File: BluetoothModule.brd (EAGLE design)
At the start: 58.4 x 30.5 mm, 25 parts, among them IC1 BL600, IC2 FT230XQ, J1 Autorun, J3 OTA, J6 USB

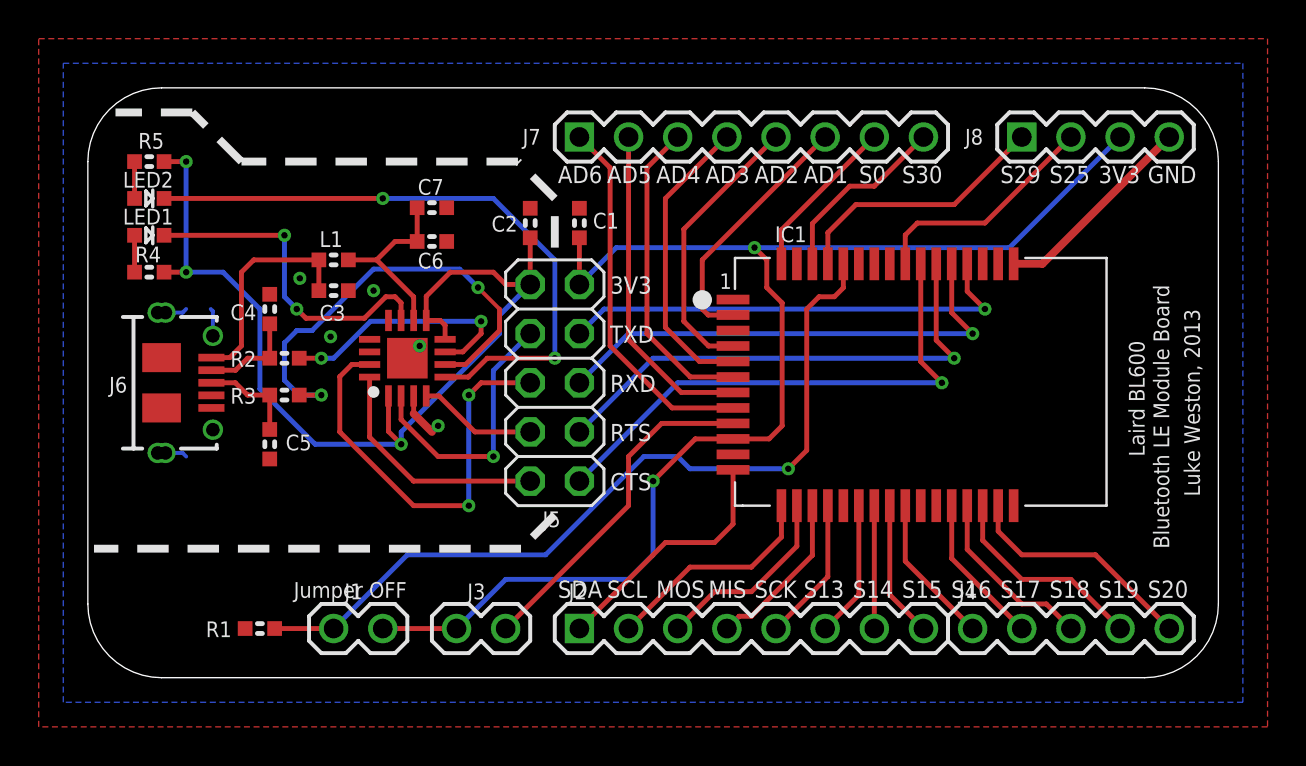
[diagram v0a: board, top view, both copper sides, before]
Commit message: tweaked USB connector footprint
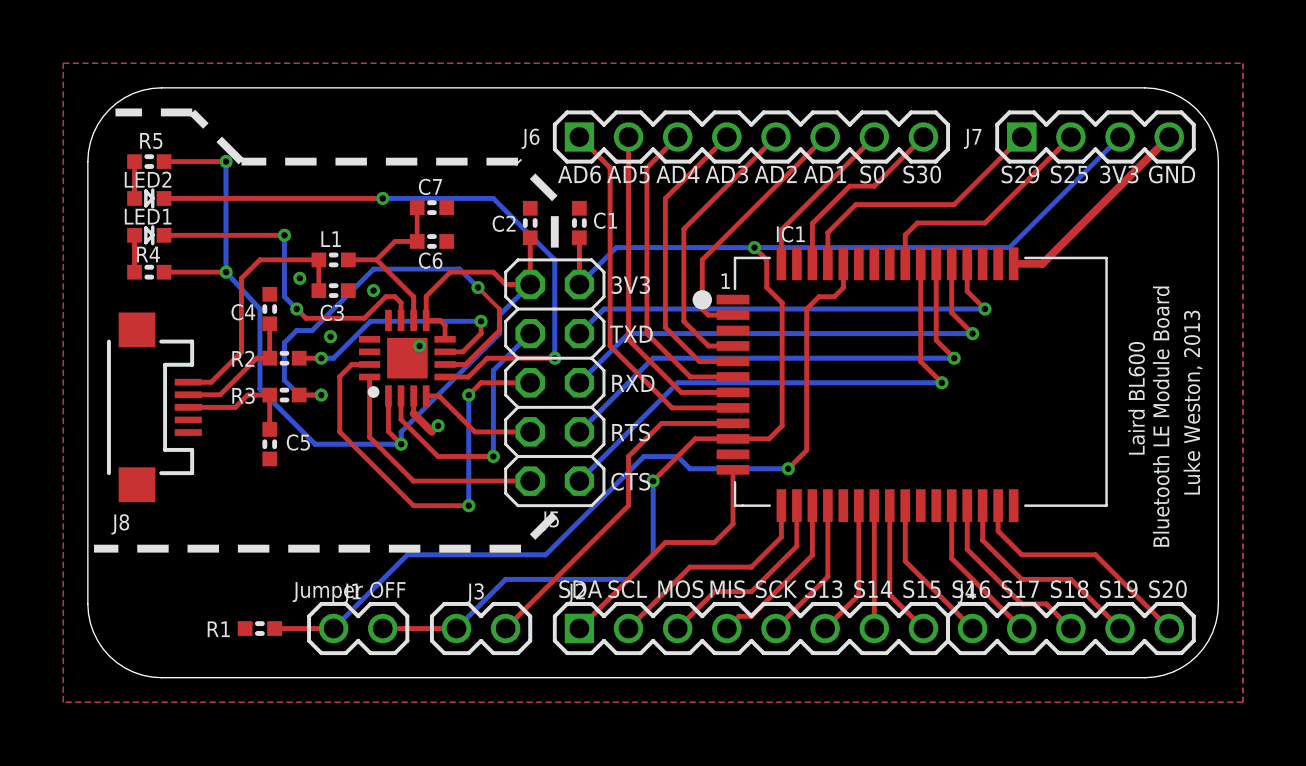
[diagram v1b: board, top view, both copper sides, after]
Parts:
- J6: value USB -> (none); device freetronics-jon:USB-MICROB-MB05PMXX -> freetronics-master-v1:1X08
- J7: device freetronics-master-v1:1X08 -> freetronics-master-v1:1X04
- J8: value (none) -> USB; device freetronics-master-v1:1X04 -> freetronics-master-v1:USB-MICROB
- moved J8 47.8 mm to (2.54, 14.0), turned to 270 degrees
- moved J6 25.0 mm to (25.4, 27.9), turned to 0 degrees
- moved J7 22.9 mm to (48.3, 27.9)
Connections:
- net +3V3: now also J7.3; no longer J8.3
- net ADC1: now also J6.6; no longer J7.6
- net ADC2: now also J6.5; no longer J7.5
- net ADC3: now also J6.4; no longer J7.4
- net ADC4: now also J6.3; no longer J7.3
- net ADC5: now also J6.2; no longer J7.2
- net ADC6: now also J6.1; no longer J7.1
- net GND: now also J7.4, J8.GND; no longer J6.FIX1, J6.FIX2, J6.GND, J6.PIN1, J6.PIN2, J6.TAB1, J6.TAB2, J8.4
- net N$11: now also J8.D-; no longer J6.D-
- net N$12: now also J8.D+; no longer J6.D+
- net N$5: now also J8.VBUS; no longer J6.VBUS
- net SIO0: now also J6.7; no longer J7.7
- net SIO25: now also J7.2; no longer J8.2
- net SIO29: now also J7.1; no longer J8.1
- net SIO30: now also J6.8; no longer J7.8
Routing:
- net GND: track 17.8 -> 13.9 mm
- net 3V3OUT: track 50.6 -> 52.7 mm
- net N$11: track 5.05 -> 6.77 mm
- net N$5: track 11.5 -> 13.2 mm
- net N$12: track 5.05 -> 6.25 mm
